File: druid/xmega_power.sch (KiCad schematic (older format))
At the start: 13 parts, among them P8 CONN_01X02, P9 CONN_01X02, U4 XC6206P332MR

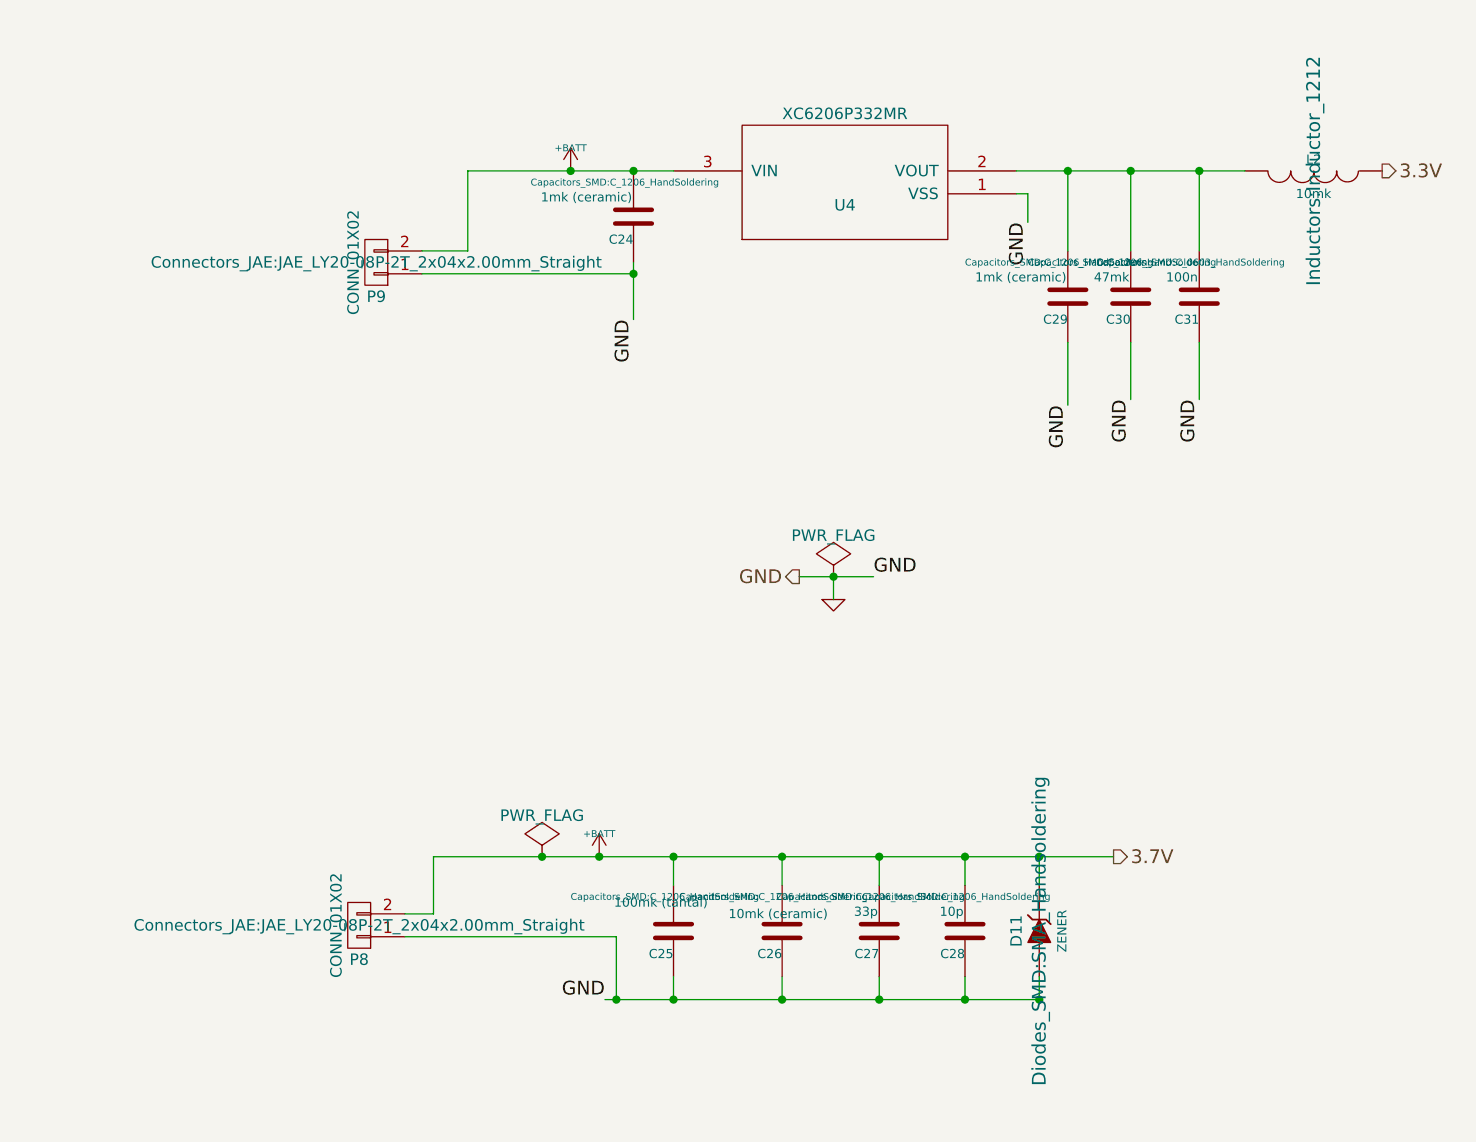
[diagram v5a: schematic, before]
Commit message: Соединеты проводникаи отдельные блоки и начато подключение SIM800 к XMEGA
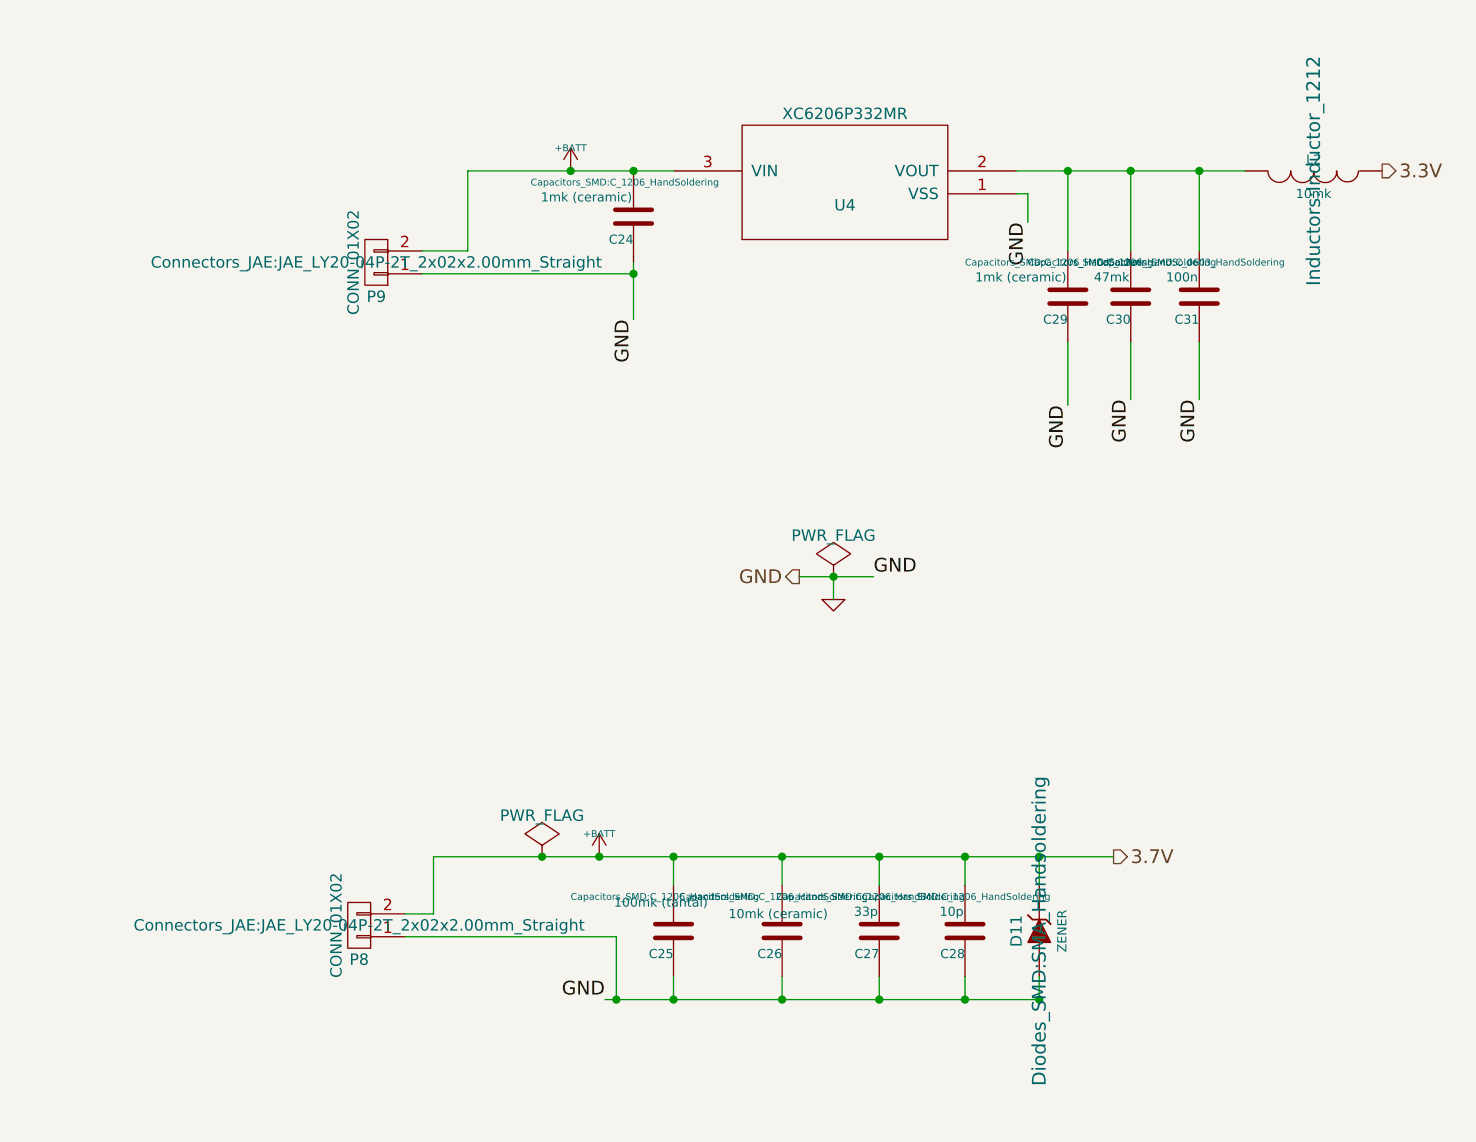
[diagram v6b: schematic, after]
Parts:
- P8, P9: footprint Connectors_JAE:JAE_LY20-08P-2T_2x04x2.00mm_Straight -> Connectors_JAE:JAE_LY20-04P-2T_2x02x2.00mm_Straight
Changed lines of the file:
@@
 F 0 "P9" H 3650 2800 50  0000 C CNN
 F 1 "CONN_01X02" V 3750 2650 50  0000 C CNN
-F 2 "Connectors_JAE:JAE_LY20-08P-2T_2x04x2.00mm_Straight" H 3650 2650 50  0000 C CNN
+F 2 "Connectors_JAE:JAE_LY20-04P-2T_2x02x2.00mm_Straight" H 3650 2650 50  0000 C CNN
 F 3 "" H 3650 2650 50  0000 C CNN
 	1    3650 2650
@@
 F 0 "P8" H 3575 5700 50  0000 C CNN
 F 1 "CONN_01X02" V 3675 5550 50  0000 C CNN
-F 2 "Connectors_JAE:JAE_LY20-08P-2T_2x04x2.00mm_Straight" H 3575 5550 50  0000 C CNN
+F 2 "Connectors_JAE:JAE_LY20-04P-2T_2x02x2.00mm_Straight" H 3575 5550 50  0000 C CNN
 F 3 "" H 3575 5550 50  0000 C CNN
 	1    3575 5550
